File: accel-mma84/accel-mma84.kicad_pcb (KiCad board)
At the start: 2 copper layers, 27.3 x 27.9 mm, 10 parts, among them IC1 AT24CS01-STUM, J2 CONN_01X10, J3 CONN_01X02, U1 MMA8452Q

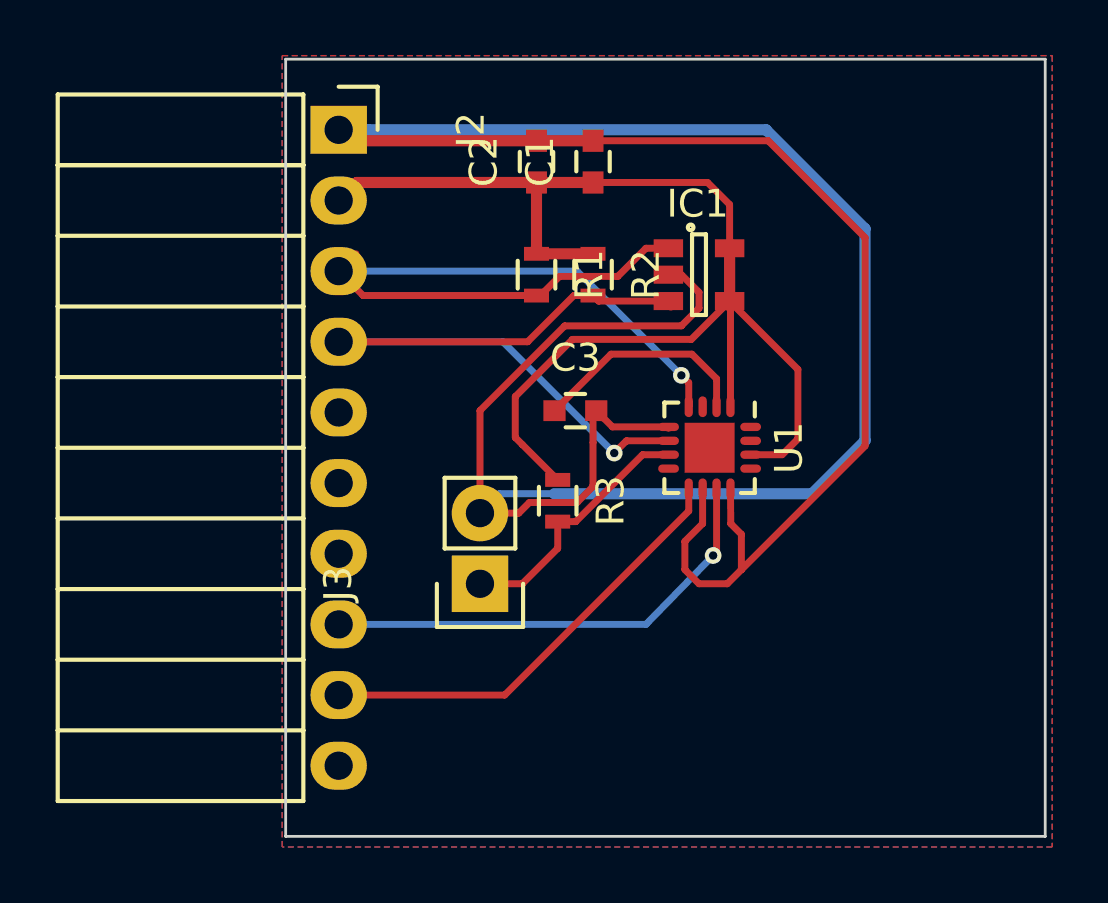
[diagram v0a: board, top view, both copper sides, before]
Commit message: Adds a bridge for disabling write protection.
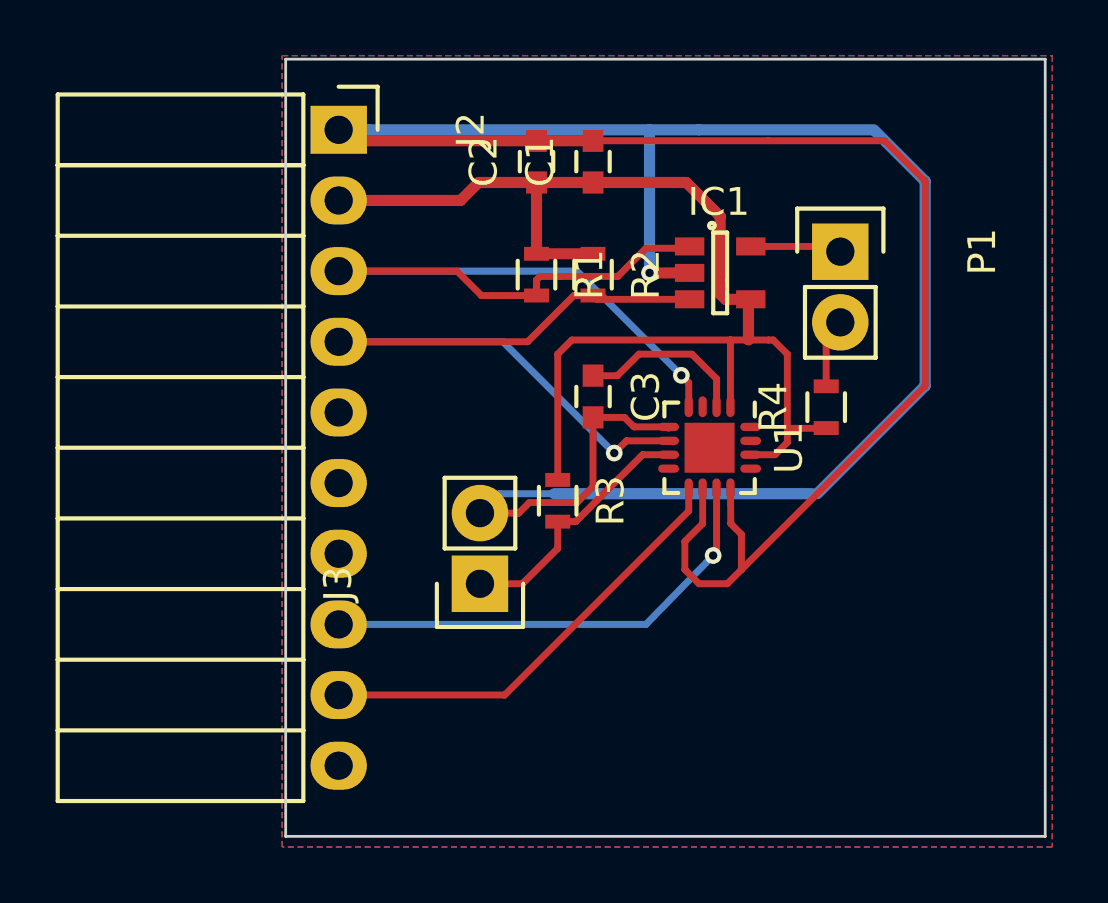
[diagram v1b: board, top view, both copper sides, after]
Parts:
- added P1: CONN_01X02, Socket_Strips:Socket_Strip_Straight_1x02, F.Cu at (142.5, 97.7)
- added R4: R, Resistors_SMD:R_0603, F.Cu at (142.0, 103.3)
- moved C3 0.81 mm to (133.6, 102.9), turned to 270 degrees
- moved IC1 0.76 mm to (138.2, 98.5)
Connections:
- IC1 pad 5: VCC -> Net-(IC1-Pad5)
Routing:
- net Net-(IC1-Pad5): track 0.00 -> 3.30 mm
- net Net-(P1-Pad2): track 0.00 -> 2.51 mm
- net Net-(C3-Pad1): track 8.04 -> 6.13 mm
- net VCC: track 48.1 -> 46.6 mm
- net GND: vias 0 -> 1

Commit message: Updates footprint
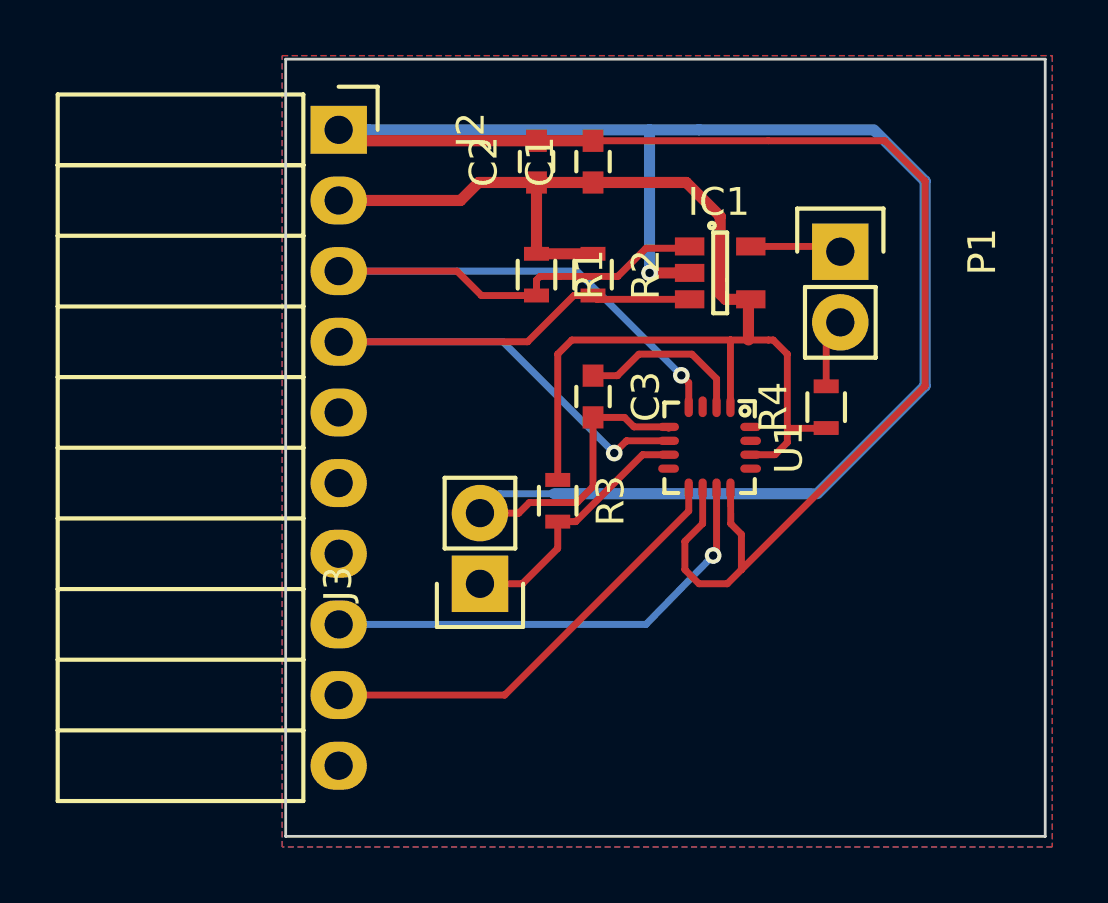
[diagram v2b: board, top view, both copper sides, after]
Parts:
- U1: footprint Housings_DFN_QFN:QFN-16-1EP_3x3mm_Pitch0.5mm -> tessel:QFN-16-1EP_3x3mm_Pitch0.5mm
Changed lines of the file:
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@@
     (links 30)
     (no_connects 0)
-    (area 113.634999 90.678 150.702334 119.126001)
+    (area -4.275 -3.975 150.702334 119.126001)
     (thickness 1.6)
     (drawings 4)
@@
     )
   )
-  (module Housings_DFN_QFN:QFN-16-1EP_3x3mm_Pitch0.5mm (layer F.Cu)
-    (at 137.795 104.775 270)
-    (descr "16-Lead Plastic Quad Flat, No Lead Package (NG) - 3x3x0.9 mm Body [QFN]; (see Microchip Packaging Specification 00000049BS.pdf)")
-    (tags "QFN 0.5")
-    (attr smd)
-    (fp_text reference U1 (at 0 -2.85 270) (layer F.SilkS)
-      (effects (font (size 1 1) (thickness 0.15)))
-    )
-    (fp_text value MMA8452Q (at 0 2.85 270) (layer F.Fab)
-      (effects (font (size 1 1) (thickness 0.15)))
-    )
-    (fp_line (start -2.1 -2.1) (end -2.1 2.1) (layer F.CrtYd) (width 0.05))
-    (fp_line (start 2.1 -2.1) (end 2.1 2.1) (layer F.CrtYd) (width 0.05))
-    (fp_line (start -2.1 -2.1) (end 2.1 -2.1) (layer F.CrtYd) (width 0.05))
-    (fp_line (start -2.1 2.1) (end 2.1 2.1) (layer F.CrtYd) (width 0.05))
-    (fp_line (start 1.625 -1.625) (end 1.625 -1.125) (layer F.SilkS) (width 0.15))
-    (fp_line (start -1.625 1.625) (end -1.625 1.125) (layer F.SilkS) (width 0.15))
-    (fp_line (start 1.625 1.625) (end 1.625 1.125) (layer F.SilkS) (width 0.15))
-    (fp_line (start -1.625 -1.625) (end -1.125 -1.625) (layer F.SilkS) (width 0.15))
-    (fp_line (start -1.625 1.625) (end -1.125 1.625) (layer F.SilkS) (width 0.15))
-    (fp_line (start 1.625 1.625) (end 1.125 1.625) (layer F.SilkS) (width 0.15))
-    (fp_line (start 1.625 -1.625) (end 1.125 -1.625) (layer F.SilkS) (width 0.15))
-    (pad 1 smd oval (at -1.475 -0.75 270) (size 0.75 0.3) (layers F.Cu F.Paste F.Mask)
-      (net 1 VCC))
-    (pad 2 smd oval (at -1.475 -0.25 270) (size 0.75 0.3) (layers F.Cu F.Paste F.Mask)
-      (net 3 "Net-(C3-Pad1)"))
-    (pad 3 smd oval (at -1.475 0.25 270) (size 0.75 0.3) (layers F.Cu F.Paste F.Mask))
-    (pad 4 smd oval (at -1.475 0.75 270) (size 0.75 0.3) (layers F.Cu F.Paste F.Mask)
-      (net 4 SCL))
-    (pad 5 smd oval (at -0.75 1.475) (size 0.75 0.3) (layers F.Cu F.Paste F.Mask)
-      (net 2 GND))
-    (pad 6 smd oval (at -0.25 1.475) (size 0.75 0.3) (layers F.Cu F.Paste F.Mask)
-      (net 5 SDA))
-    (pad 7 smd oval (at 0.25 1.475) (size 0.75 0.3) (layers F.Cu F.Paste F.Mask)
-      (net 8 "Net-(J3-Pad1)"))
-    (pad 8 smd oval (at 0.75 1.475) (size 0.75 0.3) (layers F.Cu F.Paste F.Mask))
-    (pad 9 smd oval (at 1.475 0.75 270) (size 0.75 0.3) (layers F.Cu F.Paste F.Mask)
-      (net 7 INT2))
-    (pad 10 smd oval (at 1.475 0.25 270) (size 0.75 0.3) (layers F.Cu F.Paste F.Mask)
-      (net 2 GND))
-    (pad 11 smd oval (at 1.475 -0.25 270) (size 0.75 0.3) (layers F.Cu F.Paste F.Mask)
-      (net 6 INT1))
-    (pad 12 smd oval (at 1.475 -0.75 270) (size 0.75 0.3) (layers F.Cu F.Paste F.Mask)
-      (net 2 GND))
-    (pad 13 smd oval (at 0.75 -1.475) (size 0.75 0.3) (layers F.Cu F.Paste F.Mask))
-    (pad 14 smd oval (at 0.25 -1.475) (size 0.75 0.3) (layers F.Cu F.Paste F.Mask)
-      (net 1 VCC))
-    (pad 15 smd oval (at -0.25 -1.475) (size 0.75 0.3) (layers F.Cu F.Paste F.Mask))
-    (pad 16 smd oval (at -0.75 -1.475) (size 0.75 0.3) (layers F.Cu F.Paste F.Mask))
-    (pad 17 smd rect (at 0.45 0.45 270) (size 0.9 0.9) (layers F.Cu F.Paste F.Mask)
-      (solder_paste_margin_ratio -0.2))
-    (pad 17 smd rect (at 0.45 -0.45 270) (size 0.9 0.9) (layers F.Cu F.Paste F.Mask)
-      (solder_paste_margin_ratio -0.2))
-    (pad 17 smd rect (at -0.45 0.45 270) (size 0.9 0.9) (layers F.Cu F.Paste F.Mask)
-      (solder_paste_margin_ratio -0.2))
-    (pad 17 smd rect (at -0.45 -0.45 270) (size 0.9 0.9) (layers F.Cu F.Paste F.Mask)
-      (solder_paste_margin_ratio -0.2))
-    (model Housings_DFN_QFN.3dshapes/QFN-16-1EP_3x3mm_Pitch0.5mm.wrl
-      (at (xyz 0 0 0))
-      (scale (xyz 1 1 1))
-      (rotate (xyz 0 0 0))
-    )
-  )
   (module Housings_SOT-23_SOT-143_TSOT-6:SOT-23-5 (layer F.Cu)
     (at 138.176 98.4885)
@@
       (at (xyz 0 0 0))
       (scale (xyz 1 1 1))
+      (rotate (xyz 0 0 0))
+    )
+  )
+  (module tessel:QFN-16-1EP_3x3mm_Pitch0.5mm (layer F.Cu)
+    (at 137.795 104.775 270)
+    (descr "16-Lead Plastic Quad Flat, No Lead Package (NG) - 3x3x0.9 mm Body [QFN]; (see Microchip Packaging Specification 00000049BS.pdf)")
+    (tags "QFN 0.5")
+    (attr smd)
+    (fp_text reference U1 (at 0 -2.85 270) (layer F.SilkS)
+      (effects (font (size 1 1) (thickness 0.15)))
+    )
+    (fp_text value MMA8452Q (at 0 2.85 270) (layer F.Fab)
+      (effects (font (size 1 1) (thickness 0.15)))
+    )
+    (fp_line (start -1.6764 -1.0668) (end -1.6764 -1.6256) (layer F.SilkS) (width 0.15))
+    (fp_circle (center -1.3208 -1.27) (end -1.1684 -1.2192) (layer F.SilkS) (width 0.15))
+    (fp_line (start -2.1 -2.1) (end -2.1 2.1) (layer F.CrtYd) (width 0.05))
+    (fp_line (start 2.1 -2.1) (end 2.1 2.1) (layer F.CrtYd) (width 0.05))
+    (fp_line (start -2.1 -2.1) (end 2.1 -2.1) (layer F.CrtYd) (width 0.05))
+    (fp_line (start -2.1 2.1) (end 2.1 2.1) (layer F.CrtYd) (width 0.05))
+    (fp_line (start 1.625 -1.625) (end 1.625 -1.125) (layer F.SilkS) (width 0.15))
+    (fp_line (start -1.625 1.625) (end -1.625 1.125) (layer F.SilkS) (width 0.15))
+    (fp_line (start 1.625 1.625) (end 1.625 1.125) (layer F.SilkS) (width 0.15))
+    (fp_line (start -1.625 -1.625) (end -1.125 -1.625) (layer F.SilkS) (width 0.15))
+    (fp_line (start -1.625 1.625) (end -1.125 1.625) (layer F.SilkS) (width 0.15))
+    (fp_line (start 1.625 1.625) (end 1.125 1.625) (layer F.SilkS) (width 0.15))
+    (fp_line (start 1.625 -1.625) (end 1.125 -1.625) (layer F.SilkS) (width 0.15))
+    (pad 1 smd oval (at -1.475 -0.75 270) (size 0.75 0.3) (layers F.Cu F.Paste F.Mask)
+      (net 1 VCC))
+    (pad 2 smd oval (at -1.475 -0.25 270) (size 0.75 0.3) (layers F.Cu F.Paste F.Mask)
+      (net 3 "Net-(C3-Pad1)"))
+    (pad 3 smd oval (at -1.475 0.25 270) (size 0.75 0.3) (layers F.Cu F.Paste F.Mask))
+    (pad 4 smd oval (at -1.475 0.75 270) (size 0.75 0.3) (layers F.Cu F.Paste F.Mask)
+      (net 4 SCL))
+    (pad 5 smd oval (at -0.75 1.475) (size 0.75 0.3) (layers F.Cu F.Paste F.Mask)
+      (net 2 GND))
+    (pad 6 smd oval (at -0.25 1.475) (size 0.75 0.3) (layers F.Cu F.Paste F.Mask)
+      (net 5 SDA))
+    (pad 7 smd oval (at 0.25 1.475) (size 0.75 0.3) (layers F.Cu F.Paste F.Mask)
+      (net 8 "Net-(J3-Pad1)"))
+    (pad 8 smd oval (at 0.75 1.475) (size 0.75 0.3) (layers F.Cu F.Paste F.Mask))
+    (pad 9 smd oval (at 1.475 0.75 270) (size 0.75 0.3) (layers F.Cu F.Paste F.Mask)
+      (net 7 INT2))
+    (pad 10 smd oval (at 1.475 0.25 270) (size 0.75 0.3) (layers F.Cu F.Paste F.Mask)
+      (net 2 GND))
+    (pad 11 smd oval (at 1.475 -0.25 270) (size 0.75 0.3) (layers F.Cu F.Paste F.Mask)
+      (net 6 INT1))
+    (pad 12 smd oval (at 1.475 -0.75 270) (size 0.75 0.3) (layers F.Cu F.Paste F.Mask)
+      (net 2 GND))
+    (pad 13 smd oval (at 0.75 -1.475) (size 0.75 0.3) (layers F.Cu F.Paste F.Mask))
+    (pad 14 smd oval (at 0.25 -1.475) (size 0.75 0.3) (layers F.Cu F.Paste F.Mask)
+      (net 1 VCC))
+    (pad 15 smd oval (at -0.25 -1.475) (size 0.75 0.3) (layers F.Cu F.Paste F.Mask))
+    (pad 16 smd oval (at -0.75 -1.475) (size 0.75 0.3) (layers F.Cu F.Paste F.Mask))
+    (model Housings_DFN_QFN.3dshapes/QFN-16-1EP_3x3mm_Pitch0.5mm.wrl
+      (at (xyz 0 0 0))
+      (scale (xyz 1 1 1))

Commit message: Corrects trace widths.
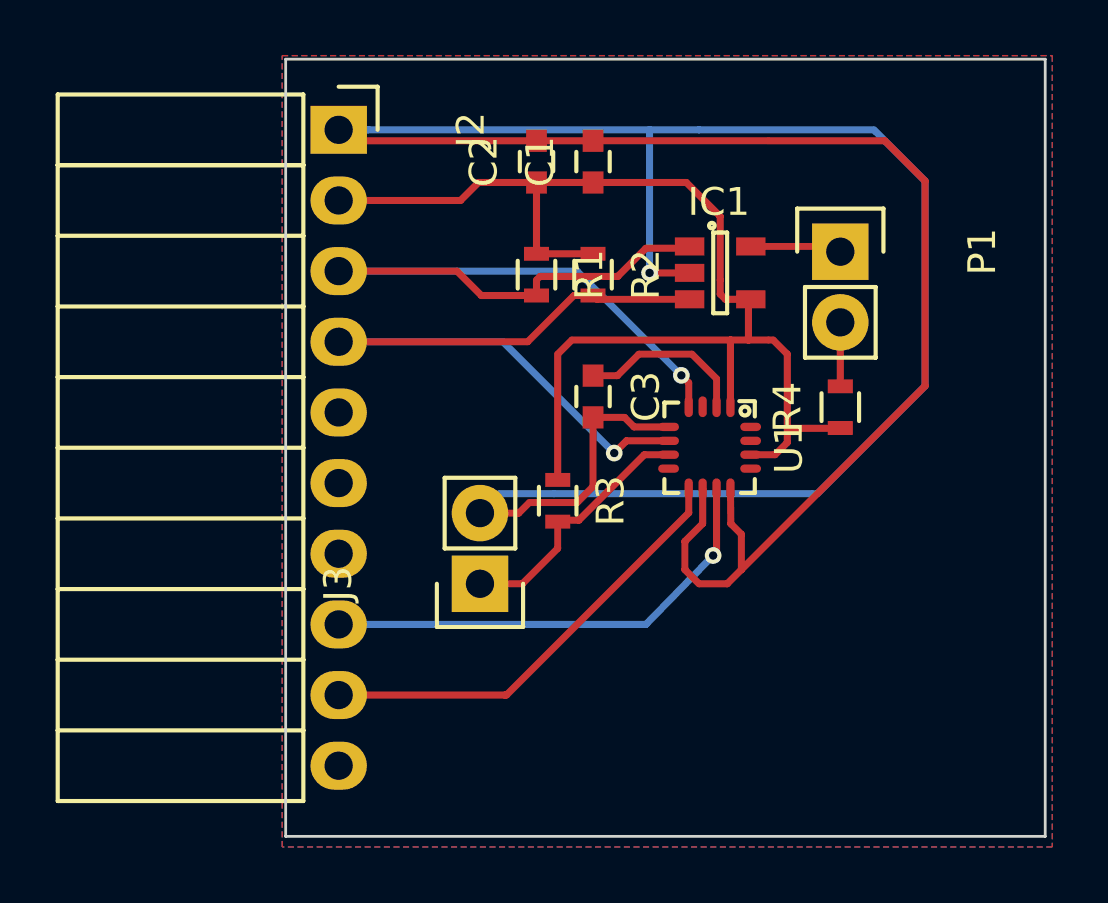
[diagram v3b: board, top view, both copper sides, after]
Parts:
- moved R4 0.51 mm to (142.5, 103.3)
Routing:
- net VCC: track 46.6 -> 47.2 mm
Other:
- net class Default: clearance 0.2 -> 0.2032; trace_width 0.25 -> 0.254
- net class Power removed
- rule trace_clearance: 0.2 -> 0.2032
